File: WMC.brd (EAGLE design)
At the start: 110 x 115 mm, 64 parts, among them IC5 MCP2551, IC6 MCP2515, IC7 ATMEGA32U4NT-TQFP, J1 LEFT MOTOR, J10 XT30F, J11 USB-B-PTH, J12 RoboClaw, J2 RIGHT MOTOR, J3 M01-2.5MM, J4 M01-2.5MM, J5 M01-2.5MM, J6 M01-2.5MM, J7 M01-2.5MM, J8 M01-2.5MM, J9 XT30F, Q1 NTD5867NLT4G, Q2 NTD5867NLT4G

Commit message: Routing, ERC, DRC for v1.0 release
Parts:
- D2, D3: value (none) -> SS56
- D4, D5: value (none) -> 1N4148
- LED1, LED2: value (none) -> RED
- moved F2 80.5 mm to (89.0, 33.0), turned to 180 degrees
- moved JP1 80.2 mm to (82.5, 41.0)
- moved JP2 80.2 mm to (85.0, 41.0)
- moved JP5 80.2 mm to (93.0, 40.5)
- moved R34 80.2 mm to (94.0, 46.0)
- moved R26 79.2 mm to (86.0, 55.0), turned to 0 degrees
- moved C15 75.8 mm to (94.0, 71.0)
- moved C16 75.8 mm to (94.0, 65.0)
- moved XTL4 75.8 mm to (94.0, 68.0)
- moved D1 75.1 mm to (79.0, 97.0)
- moved IC5 74.0 mm to (86.0, 61.0), turned to 180 degrees
- moved F1 73.2 mm to (79.0, 89.0), turned to 270 degrees
- moved J11 71.0 mm to (85.0, 109.0)
- moved R23 71.0 mm to (87.0, 99.0)
- moved R24 71.0 mm to (85.0, 99.0)
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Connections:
- net 5V: now also U$6.2
- net USB+: no longer U$6.2
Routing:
- net RD-: track 16.7 -> 99.1 mm, vias 0 -> 2
- net RD+: track 17.5 -> 94.9 mm, vias 0 -> 2
- net MISO: track 47.2 -> 108.1 mm
- net SCK: track 45.5 -> 106.2 mm, vias 1 -> 2
- net MOSI: track 38.7 -> 96.1 mm
- net D2_SDA: track 25.7 -> 71.4 mm
- net USB+: track 40.4 -> 8.02 mm
- net D10_A11: track 46.8 -> 77.5 mm
- net TX_LED: track 17.3 -> 36.8 mm
- net GND: track 82.0 -> 67.2 mm, vias 26 -> 30
- net RXLED_SS: track 5.10 -> 19.5 mm
- net CANL: track 21.2 -> 34.0 mm
- net 24V: track 141.3 -> 152.3 mm
- net CANH: track 26.6 -> 37.4 mm
- net D9_A10: track 36.5 -> 26.8 mm
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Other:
- board size 110 x 115 mm -> 100 x 115 mm
- board text added: "Arduino Leonardo compatible"
- board text removed: "5V"

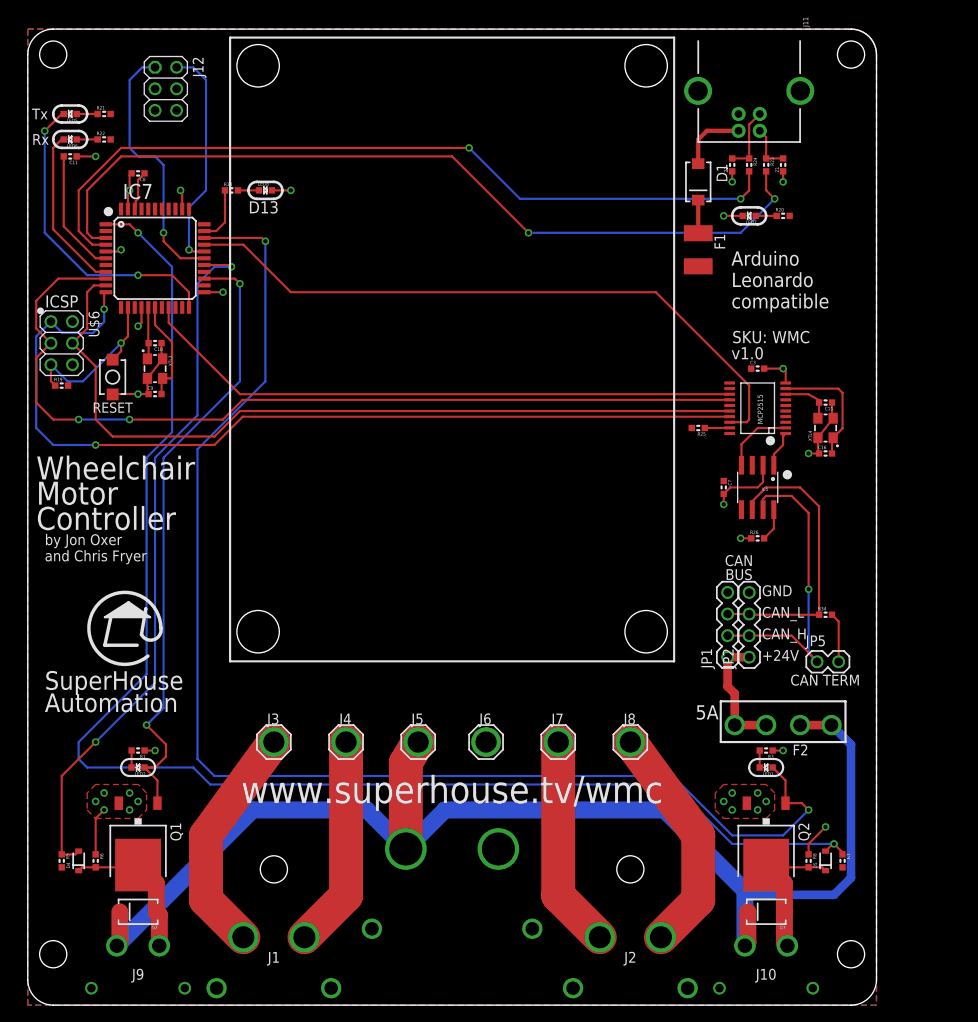
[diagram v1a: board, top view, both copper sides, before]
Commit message: Changed lock status LEDs to green to indicate chair will move when locks released - green means go
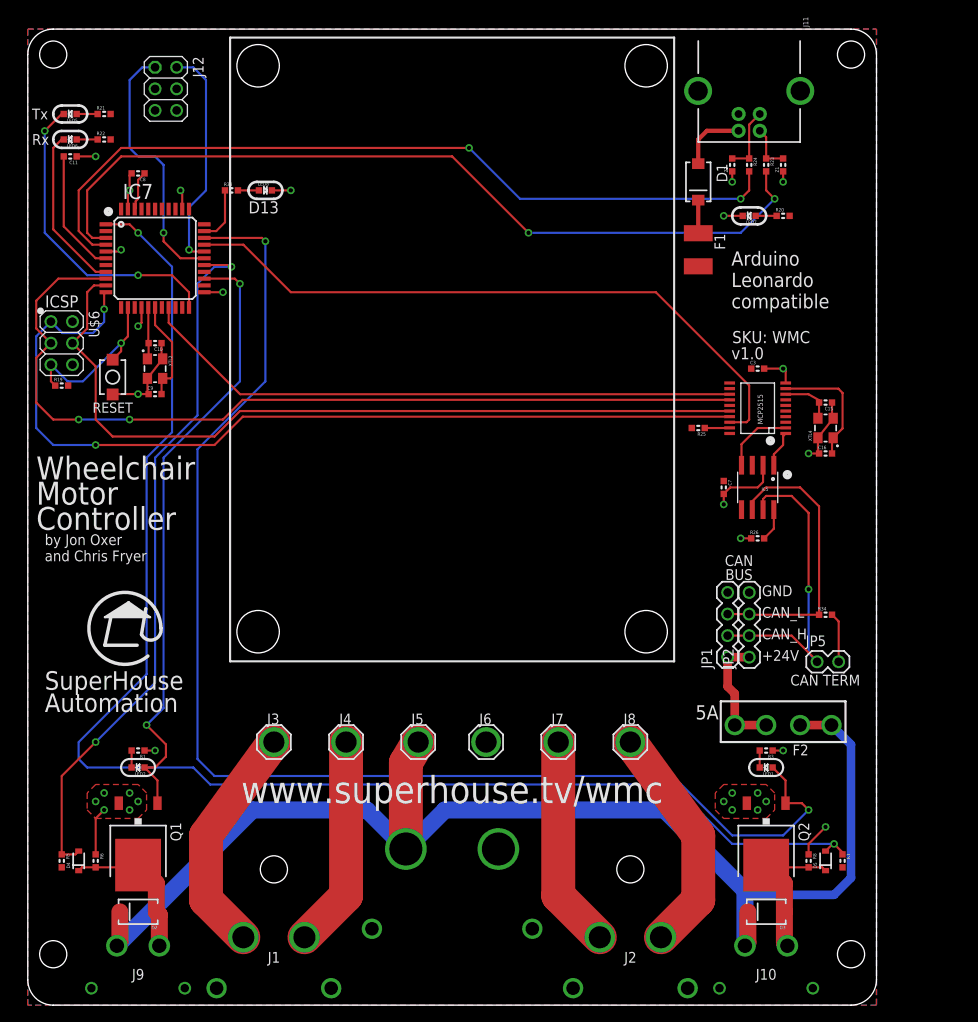
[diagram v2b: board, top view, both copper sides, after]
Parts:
- LED1, LED2: value RED -> GREEN
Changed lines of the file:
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@@
 <attribute name="VALUE" x="-2.445" y="81.81" size="1.27" layer="27" rot="R270"/>
 </element>
-<element name="LED1" library="SuperHouse-LEDs" library_urn="urn:adsk.eagle:library:11790571" package="LED-0603" package3d_urn="urn:adsk.eagle:package:7066240/3" value="RED" x="87" y="28" smashed="yes" rot="R180">
+<element name="LED1" library="SuperHouse-LEDs" library_urn="urn:adsk.eagle:library:11790571" package="LED-0603" package3d_urn="urn:adsk.eagle:package:7066240/3" value="GREEN" x="87" y="28" smashed="yes" rot="R180">
 <attribute name="NAME" x="87.889" y="27.4412" size="0.4064" layer="25" rot="R180"/>
 <attribute name="VALUE" x="88.016" y="28.9652" size="0.4064" layer="27" rot="R180"/>
 </element>
-<element name="LED2" library="SuperHouse-LEDs" library_urn="urn:adsk.eagle:library:11790571" package="LED-0603" package3d_urn="urn:adsk.eagle:package:7066240/3" value="RED" x="13" y="28" smashed="yes" rot="R180">
+<element name="LED2" library="SuperHouse-LEDs" library_urn="urn:adsk.eagle:library:11790571" package="LED-0603" package3d_urn="urn:adsk.eagle:package:7066240/3" value="GREEN" x="13" y="28" smashed="yes" rot="R180">
 <attribute name="NAME" x="13.889" y="27.4412" size="0.4064" layer="25" rot="R180"/>
 <attribute name="VALUE" x="14.016" y="28.9652" size="0.4064" layer="27" rot="R180"/>
@@
 <signal name="GND">
 <polygon width="0.4064" layer="16">
-<vertex x="97" y="115" curve="-90"/>
-<vertex x="100" y="112"/>
+<vertex x="100" y="115"/>
 <vertex x="100" y="0"/>
 <vertex x="0" y="0"/>
@@
 <signal name="5V">
 <polygon width="0.4064" layer="1" rank="3">
-<vertex x="97" y="115" curve="-90"/>
-<vertex x="100" y="112"/>
+<vertex x="100" y="115"/>
 <vertex x="100" y="0"/>
 <vertex x="0" y="0"/>
